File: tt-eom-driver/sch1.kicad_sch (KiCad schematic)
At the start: 9 parts

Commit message: updates to DAC circuitry
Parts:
- added IC4: TPS7A4901DRBT, TPS7A4901DRBT, symbol TPS7A4901DRBT:TPS7A4901DRBT
- added U6: TPS7A3001DRBT, DGN8_1P89x1P57_TEX, symbol TPS7A3001DRBT:TPS7A3001DRBT
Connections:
- net GND: now also IC4.10 (EP_2), IC4.11 (EP_3), IC4.12 (EP_4), IC4.13 (EP_5), IC4.4 (GND), IC4.9 (EP_1), U6.4 (GND), U6.EPAD; no longer PS1.2 (-VIN)
- new net RETURN_GND: PS1.2 (-VIN)
- no-connect marks 1 -> 3
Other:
- moved on the sheet: C37, C38, C39, C40, FB1, FB2, FB3, FB4, PS1

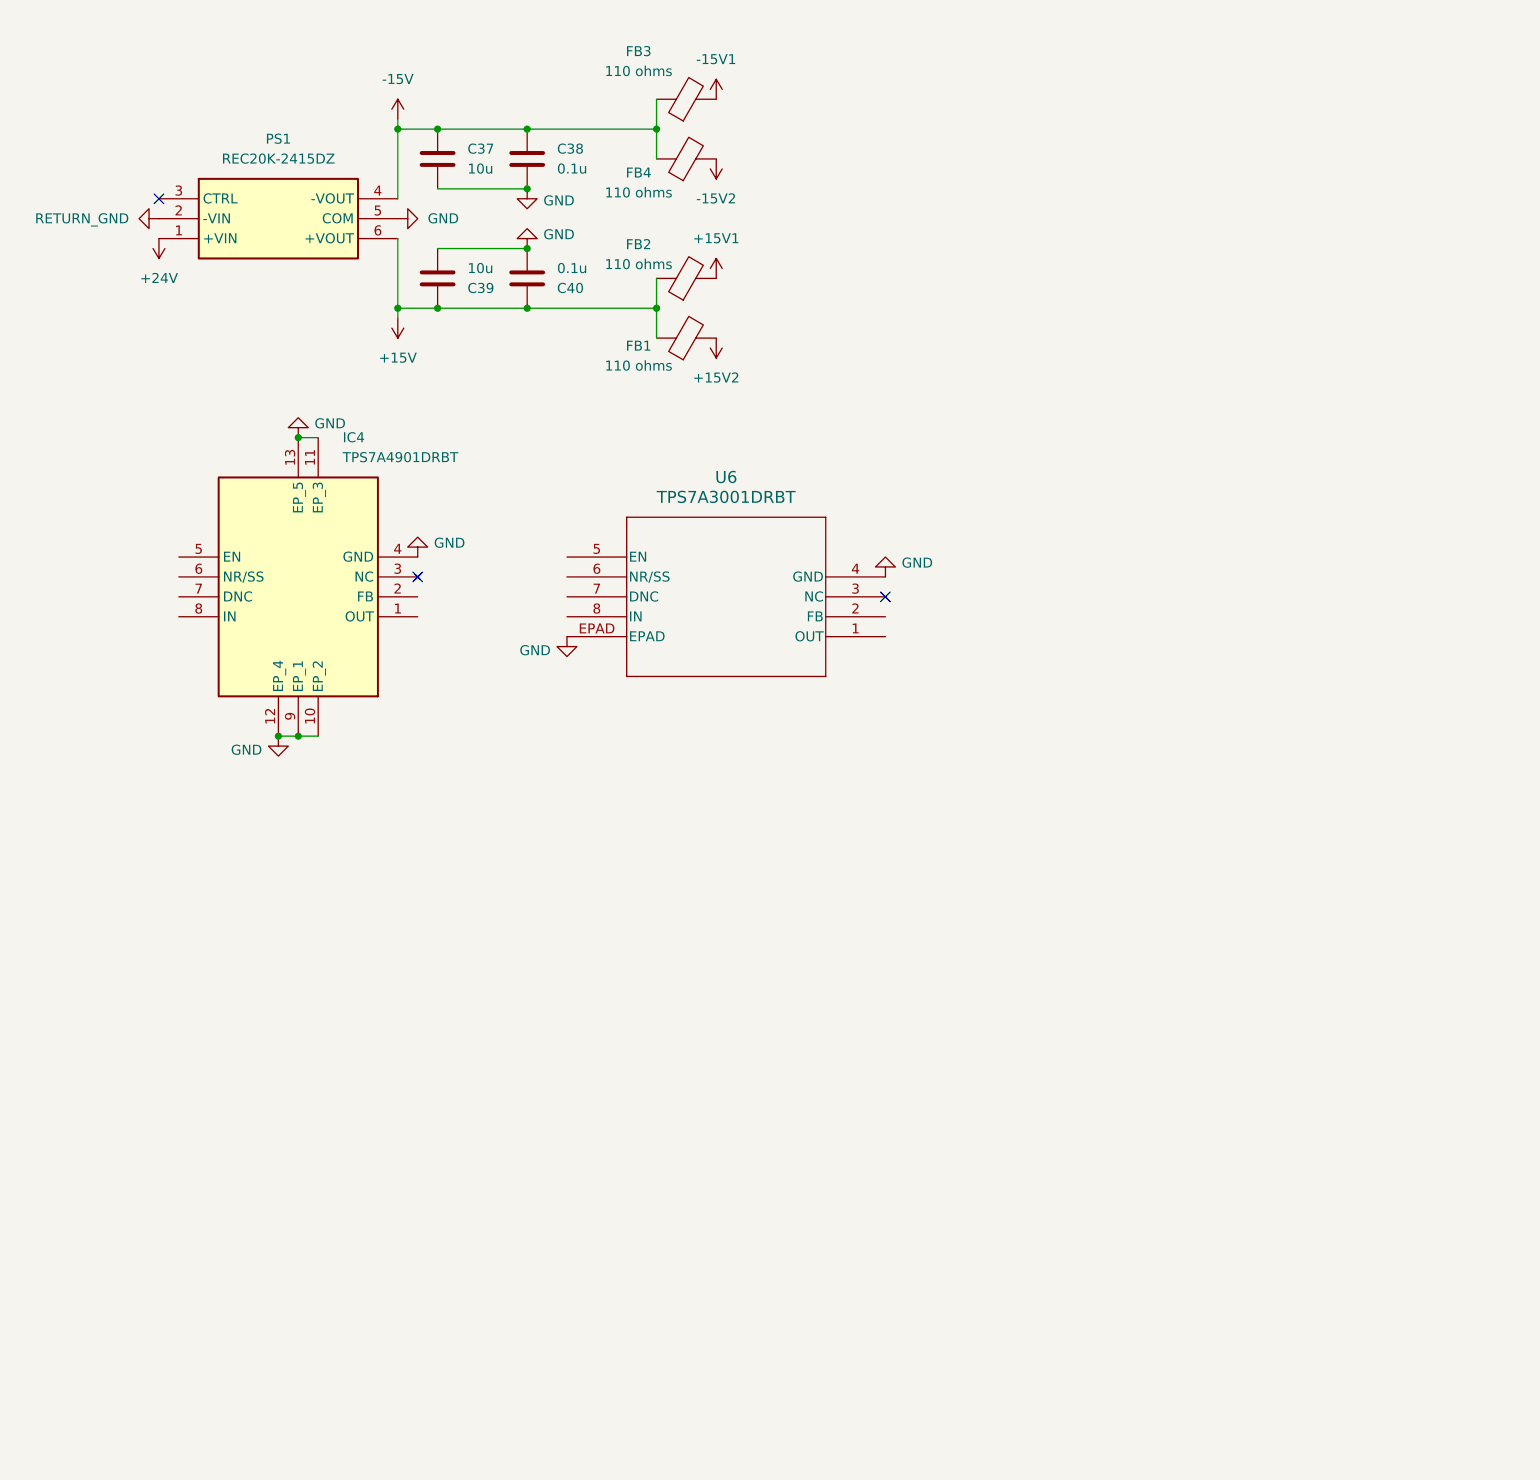
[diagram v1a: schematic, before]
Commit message: added pwr section
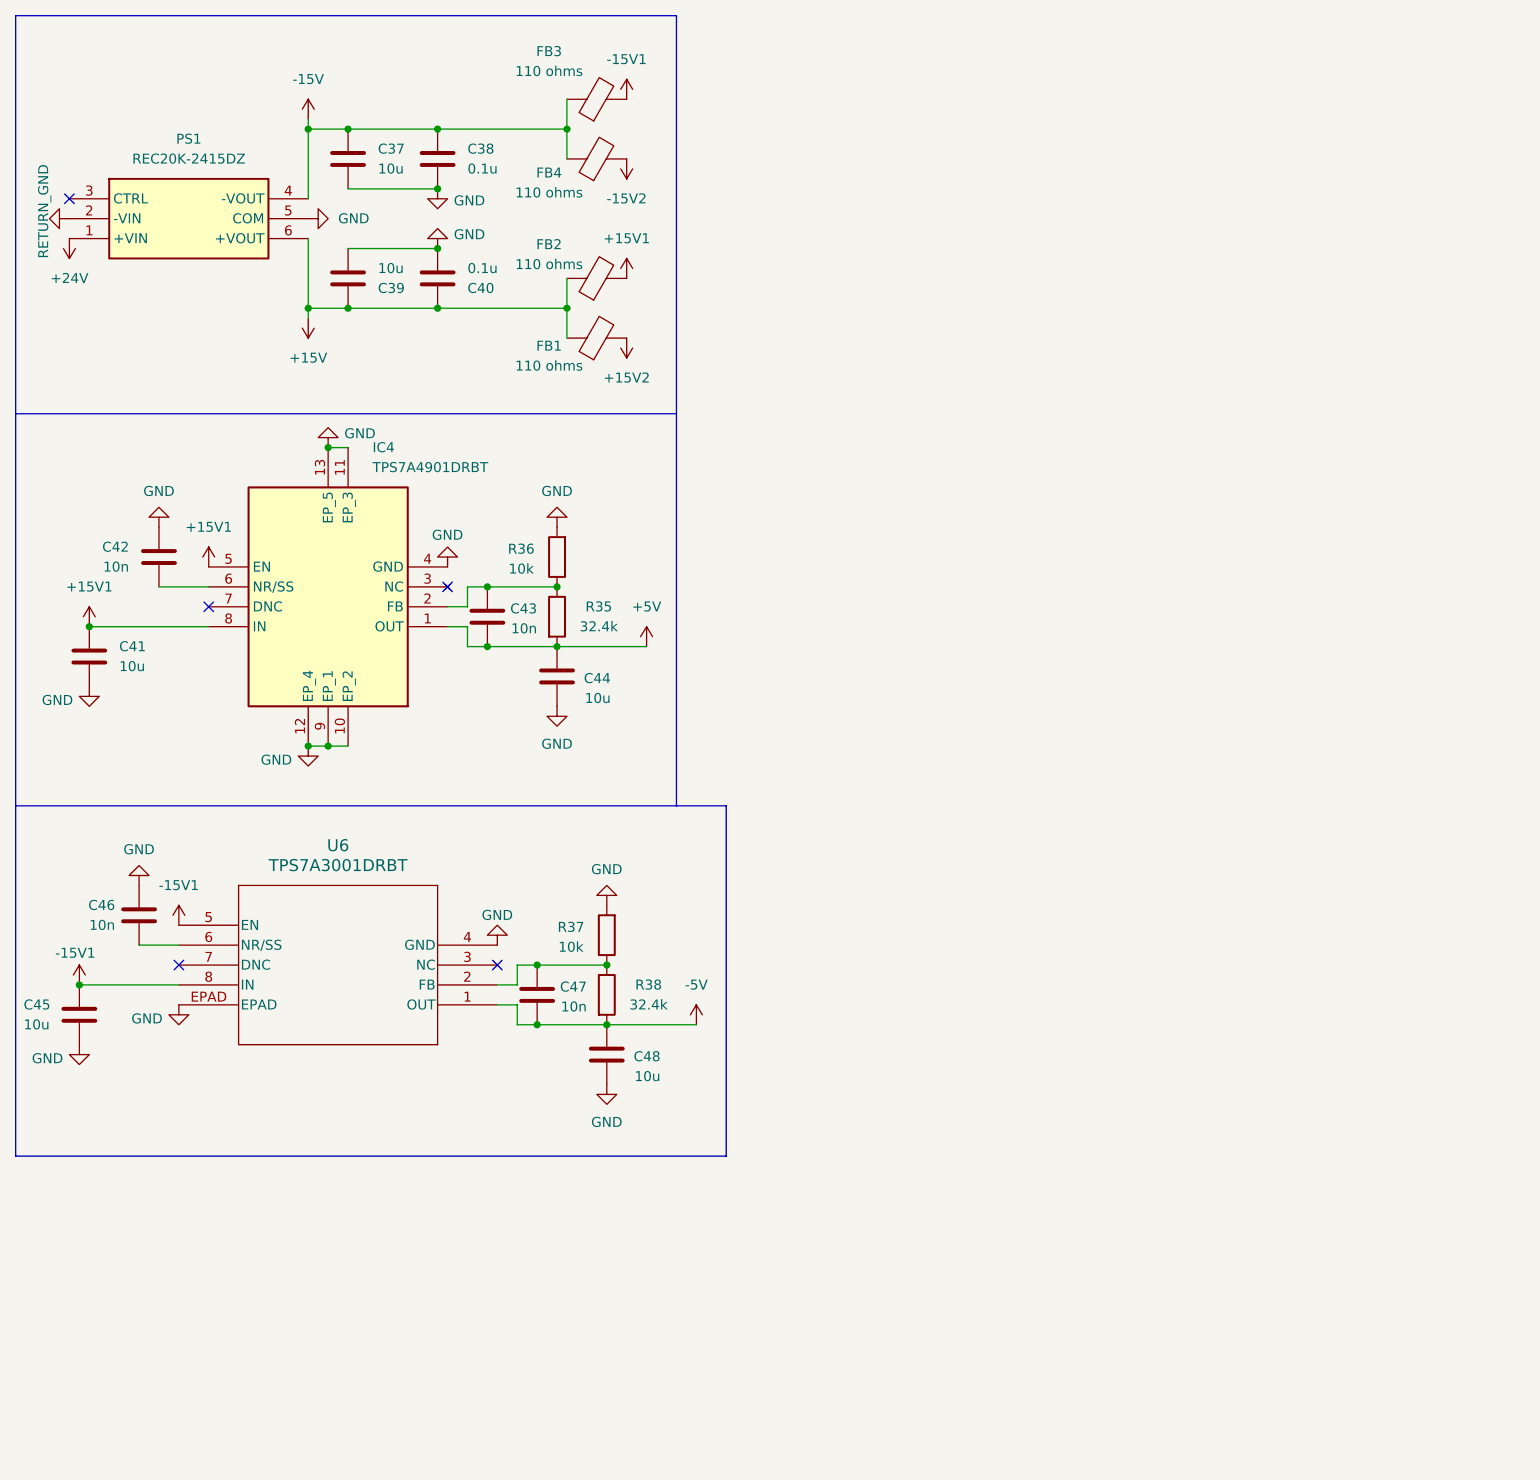
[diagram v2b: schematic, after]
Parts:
- added C41, C44, C45, C48: 10u, symbol Device:C
- added C42, C43, C46, C47: 10n, symbol Device:C
- added R35, R38: 32.4k, symbol Device:R
- added R36, R37: 10k, symbol Device:R
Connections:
- net +15V1: now also IC4.5 (EN), IC4.8 (IN), C41.1
- net -15V1: now also U6.5 (EN), U6.8 (IN), C45.1
- net GND: now also C41.2, C42.2, C44.2, C45.2, C46.2, C48.2, R36.2, R37.2
- net +5V: now reaches IC4.1 (OUT)
- net +5V: now also C43.1, C44.1, R35.2
- net at IC4.2 (FB): now also C43.2, R35.1, R36.1
- net at IC4.6 (NR/SS): now also C42.1
- net -5V: now reaches U6.1 (OUT)
- net -5V: now also C47.1, C48.1, R38.2
- net at U6.2 (FB): now also C47.2, R37.1, R38.1
- net at U6.6 (NR/SS): now also C46.1
- no-connect marks 3 -> 5
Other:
- moved on the sheet: C37, C38, C39, C40, FB1, FB2, FB3, FB4, IC4, PS1, U6

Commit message: added input pwr section
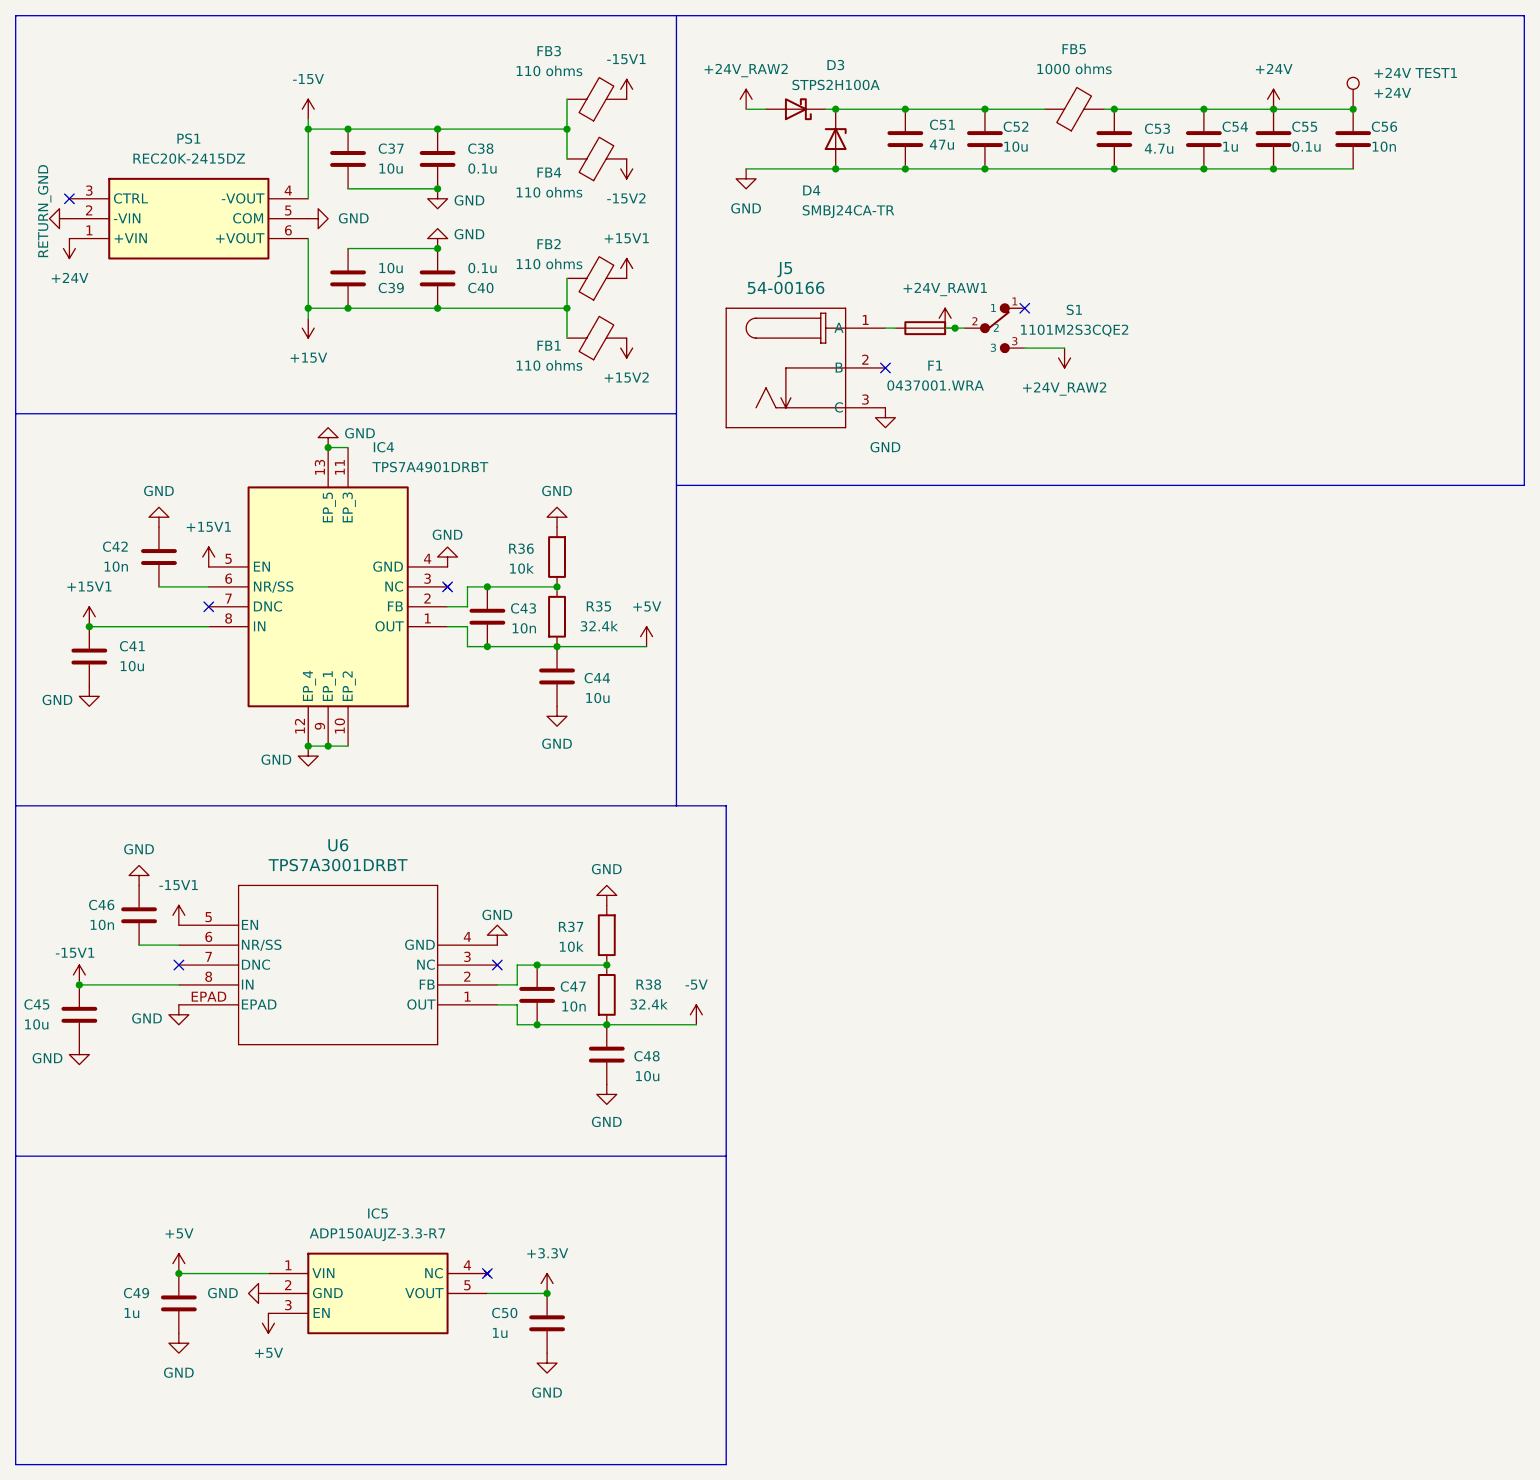
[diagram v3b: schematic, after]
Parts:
- added +24V TEST1: +24V, TestPoint:TestPoint_Keystone_5015_Micro_Mini, symbol Connector:TestPoint
- added C49, C50: 1u, symbol Device:C
- added C51: 47u, Capacitor_SMD:C_2220_5750Metric, symbol Device:C
- added C52: 10u, Capacitor_SMD:C_1210_3225Metric, symbol Device:C
- added C53: 4.7u, Capacitor_SMD:C_0805_2012Metric, symbol Device:C
- added C54: 1u, Capacitor_SMD:C_0603_1608Metric, symbol Device:C
- added C55: 0.1u, Capacitor_SMD:C_0603_1608Metric, symbol Device:C
- added C56: 10n, Capacitor_SMD:C_0603_1608Metric, symbol Device:C
- added D3: ​​​STPS2H100A, Diode_SMD:D_SMA, symbol Device:D_Schottky
- added D4: SMBJ24CA-TR, Diode_SMD:D_SMB, symbol Diode:PTVS26VZ1USK
- added F1: 0437001.WRA, Fuse:Fuse_1206_3216Metric, symbol Device:Fuse
- added FB5: 1000 ohms, Inductor_SMD:L_0603_1608Metric, symbol Device:FerriteBead
- added IC5: ADP150AUJZ-3.3-R7, SOT95P280X100-5N, symbol ADP150AUJZ-3.3-R7:ADP150AUJZ-3.3-R7
- added J5: 54-00166, 54-00166:CONN3_54-00166_TEN, symbol 54-00166:54-00166
- added S1: 1101M2S3CQE2, 1101M2S3CQE2:SW_1101M2S3CQE2, symbol 1101M2S3CQE2:1101M2S3CQE2
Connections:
- net +24V: now also +24V TEST1.1, C53.1, C54.1, C55.1, C56.1, FB5.2
- net +5V: now also C49.1, IC5.1 (VIN), IC5.3 (EN)
- net GND: now also C49.2, C50.2, C51.2, C52.2, C53.2, C54.2, C55.2, C56.2, D4.2 (A), IC5.2 (GND), J5.3 (C)
- new net: C51.1, C52.1, D3.1 (K), D4.1 (K), FB5.1
- new net: F1.1, J5.1 (A)
- new net +24V_RAW1: F1.2, S1.2
- new net +24V_RAW2: D3.2 (A), S1.3
- new net +3.3V: C50.1, IC5.5 (VOUT)
- no-connect marks 5 -> 8

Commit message: little error to DAC
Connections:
- net +15V: now also C41.1, IC4.8 (IN)
- net +15V1: no longer C41.1, IC4.8 (IN)
- net -15V: now also C45.1, U6.8 (IN)
- net -15V1: no longer C45.1, U6.8 (IN)
- net GND: no longer C51.2, C52.2, C53.2, C54.2, C55.2, C56.2, D4.2 (A), J5.3 (C)
- net RETURN_GND: now also C51.2, C52.2, C53.2, C54.2, C55.2, C56.2, D4.2 (A), J5.3 (C)
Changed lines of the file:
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@@
 			)
 		)
-		(property "Datasheet" "BLM21SP111SN1"
+		(property "Datasheet" "BLM21SP111SN1, 1206?"
 			(at 86.36 22.86 0)
 			(hide yes)
@@
 		(in_pos_files yes)
 		(dnp no)
-		(fields_autoplaced yes)
 		(property "Reference" "#PWR078"
 			(at 21.59 93.98 0)
@@
 			)
 		)
-		(property "Value" "+15V1"
-			(at 21.59 85.09 0)
+		(property "Value" "+15V"
+			(at 19.05 85.852 0)
 			(show_name no)
 			(do_not_autoplace no)
@@
 					(size 1.27 1.27)
 				)
+				(justify left)
 			)
 		)
@@
 			)
 		)
-		(property "Value" "GND"
+		(property "Value" "RETURN_GND"
 			(at 105.41 36.83 0)
 			(show_name no)
@@
 			)
 		)
-		(property "Value" "GND"
+		(property "Value" "RETURN_GND"
 			(at 123.19 67.31 0)
 			(show_name no)
@@
 			)
 		)
-		(property "Value" "-15V1"
+		(property "Value" "-15V"
 			(at 19.812 131.826 0)
 			(show_name no)
